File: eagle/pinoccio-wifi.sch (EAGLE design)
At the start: 18 parts, among them U1 LDO-TPS78233, U2 LDO-TPS73533

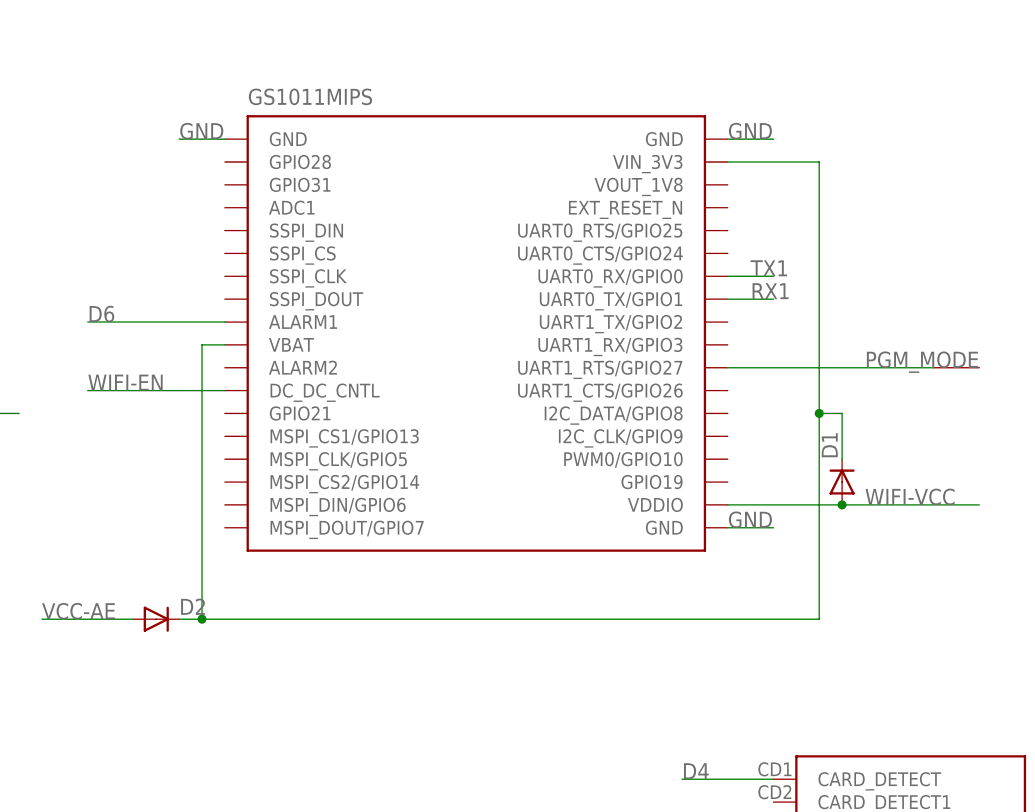
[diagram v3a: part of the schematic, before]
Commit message: Update datasheet and dioide layout to 0603
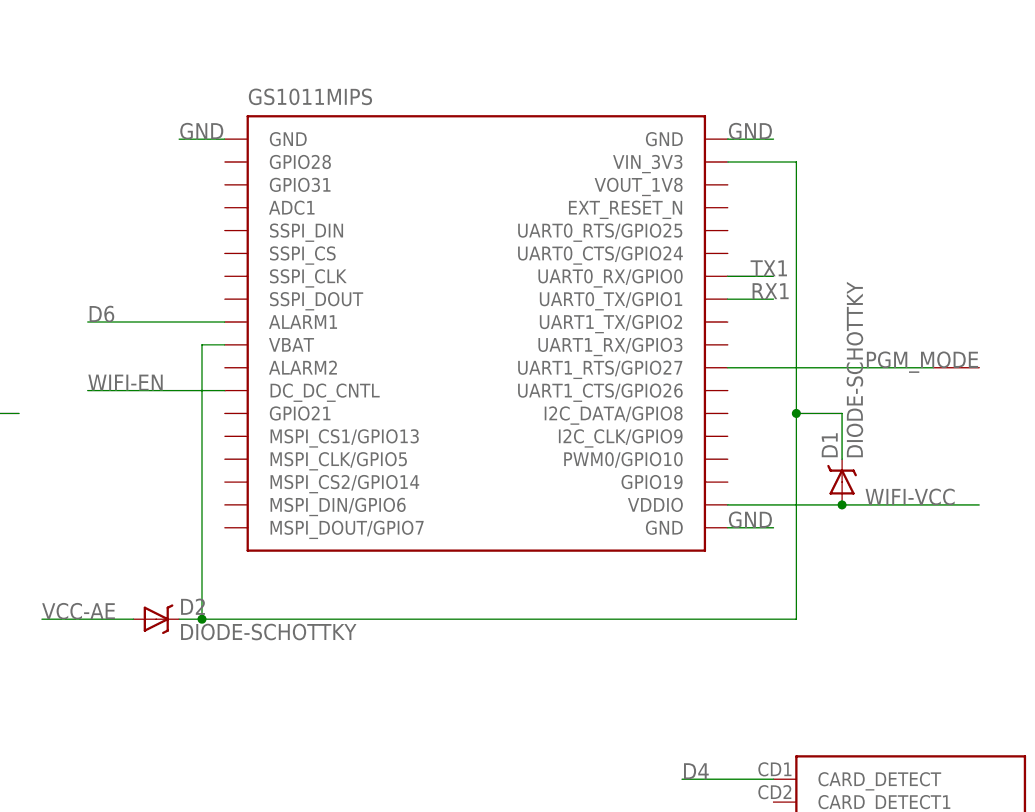
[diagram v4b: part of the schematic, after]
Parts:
- D1, D2: value (none) -> DIODE-SCHOTTKY; device Pinoccio:DIODE0603 -> Pinoccio:DIODE-SCHOTTKY
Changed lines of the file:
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@@
 <grid distance="0.1" unitdist="inch" unit="inch" style="lines" multiple="1" display="no" altdistance="0.01" altunitdist="inch" altunit="inch"/>
 <layers>
-<layer number="1" name="Top" color="4" fill="1" visible="yes" active="no"/>
-<layer number="2" name="Route2" color="1" fill="3" visible="yes" active="no"/>
-<layer number="3" name="Route3" color="4" fill="3" visible="yes" active="no"/>
-<layer number="4" name="Route4" color="1" fill="4" visible="yes" active="no"/>
-<layer number="5" name="Route5" color="4" fill="4" visible="yes" active="no"/>
-<layer number="6" name="Route6" color="1" fill="8" visible="yes" active="no"/>
-<layer number="7" name="Route7" color="4" fill="8" visible="yes" active="no"/>
-<layer number="8" name="Route8" color="1" fill="2" visible="yes" active="no"/>
-<layer number="9" name="Route9" color="4" fill="2" visible="yes" active="no"/>
-<layer number="10" name="Route10" color="1" fill="7" visible="yes" active="no"/>
-<layer number="11" name="Route11" color="4" fill="7" visible="yes" active="no"/>
-<layer number="12" name="Route12" color="1" fill="5" visible="yes" active="no"/>
-<layer number="13" name="Route13" color="4" fill="5" visible="yes" active="no"/>
-<layer number="14" name="Route14" color="1" fill="6" visible="yes" active="no"/>
-<layer number="15" name="Route15" color="4" fill="6" visible="yes" active="no"/>
-<layer number="16" name="Bottom" color="1" fill="1" visible="yes" active="no"/>
-<layer number="17" name="Pads" color="2" fill="1" visible="yes" active="no"/>
-<layer number="18" name="Vias" color="2" fill="1" visible="yes" active="no"/>
-<layer number="19" name="Unrouted" color="6" fill="1" visible="yes" active="no"/>
-<layer number="20" name="Dimension" color="6" fill="1" visible="yes" active="no"/>
-<layer number="21" name="tPlace" color="16" fill="1" visible="yes" active="no"/>
-<layer number="22" name="bPlace" color="14" fill="1" visible="yes" active="no"/>
-<layer number="23" name="tOrigins" color="15" fill="1" visible="yes" active="no"/>
-<layer number="24" name="bOrigins" color="15" fill="1" visible="yes" active="no"/>
-<layer number="25" name="tNames" color="7" fill="1" visible="yes" active="no"/>
-<layer number="26" name="bNames" color="7" fill="1" visible="yes" active="no"/>
-<layer number="27" name="tValues" color="7" fill="1" visible="yes" active="no"/>
-<layer number="28" name="bValues" color="7" fill="1" visible="yes" active="no"/>
+<layer number="1" name="Top" color="4" fill="1" visible="no" active="no"/>
+<layer number="2" name="Route2" color="1" fill="3" visible="no" active="no"/>
+<layer number="3" name="Route3" color="4" fill="3" visible="no" active="no"/>
+<layer number="4" name="Route4" color="1" fill="4" visible="no" active="no"/>
+<layer number="5" name="Route5" color="4" fill="4" visible="no" active="no"/>
+<layer number="6" name="Route6" color="1" fill="8" visible="no" active="no"/>
+<layer number="7" name="Route7" color="4" fill="8" visible="no" active="no"/>
+<layer number="8" name="Route8" color="1" fill="2" visible="no" active="no"/>
+<layer number="9" name="Route9" color="4" fill="2" visible="no" active="no"/>
+<layer number="10" name="Route10" color="1" fill="7" visible="no" active="no"/>
+<layer number="11" name="Route11" color="4" fill="7" visible="no" active="no"/>
+<layer number="12" name="Route12" color="1" fill="5" visible="no" active="no"/>
+<layer number="13" name="Route13" color="4" fill="5" visible="no" active="no"/>
+<layer number="14" name="Route14" color="1" fill="6" visible="no" active="no"/>
+<layer number="15" name="Route15" color="4" fill="6" visible="no" active="no"/>
+<layer number="16" name="Bottom" color="1" fill="1" visible="no" active="no"/>
+<layer number="17" name="Pads" color="2" fill="1" visible="no" active="no"/>
+<layer number="18" name="Vias" color="2" fill="1" visible="no" active="no"/>
+<layer number="19" name="Unrouted" color="6" fill="1" visible="no" active="no"/>
+<layer number="20" name="Dimension" color="6" fill="1" visible="no" active="no"/>
+<layer number="21" name="tPlace" color="16" fill="1" visible="no" active="no"/>
+<layer number="22" name="bPlace" color="14" fill="1" visible="no" active="no"/>
+<layer number="23" name="tOrigins" color="15" fill="1" visible="no" active="no"/>
+<layer number="24" name="bOrigins" color="15" fill="1" visible="no" active="no"/>
+<layer number="25" name="tNames" color="7" fill="1" visible="no" active="no"/>
+<layer number="26" name="bNames" color="7" fill="1" visible="no" active="no"/>
+<layer number="27" name="tValues" color="7" fill="1" visible="no" active="no"/>
+<layer number="28" name="bValues" color="7" fill="1" visible="no" active="no"/>
 <layer number="29" name="tStop" color="5" fill="1" visible="no" active="no"/>
 <layer number="30" name="bStop" color="7" fill="6" visible="no" active="no"/>
@@
 <layer number="35" name="tGlue" color="7" fill="4" visible="no" active="no"/>
 <layer number="36" name="bGlue" color="7" fill="5" visible="no" active="no"/>
-<layer number="37" name="tTest" color="7" fill="1" visible="yes" active="no"/>
-<layer number="38" name="bTest" color="7" fill="1" visible="yes" active="no"/>
+<layer number="37" name="tTest" color="7" fill="1" visible="no" active="no"/>
+<layer number="38" name="bTest" color="7" fill="1" visible="no" active="no"/>
 <layer number="39" name="tKeepout" color="4" fill="11" visible="no" active="no"/>
 <layer number="40" name="bKeepout" color="1" fill="11" visible="no" active="no"/>
@@
 <layer number="44" name="Drills" color="7" fill="1" visible="no" active="no"/>
 <layer number="45" name="Holes" color="7" fill="1" visible="no" active="no"/>
-<layer number="46" name="Milling" color="3" fill="1" visible="yes" active="no"/>
-<layer number="47" name="Measures" color="7" fill="1" visible="yes" active="no"/>
-<layer number="48" name="Document" color="7" fill="1" visible="yes" active="no"/>
-<layer number="49" name="Reference" color="7" fill="1" visible="yes" active="no"/>
-<layer number="50" name="dxf" color="7" fill="1" visible="yes" active="no"/>
-<layer number="51" name="tDocu" color="6" fill="1" visible="yes" active="no"/>
-<layer number="52" name="bDocu" color="7" fill="1" visible="yes" active="no"/>
-<layer number="53" name="tGND_GNDA" color="7" fill="9" visible="yes" active="no"/>
-<layer number="54" name="bGND_GNDA" color="1" fill="9" visible="yes" active="no"/>
-<layer number="56" name="wert" color="7" fill="1" visible="yes" active="no"/>
+<layer number="46" name="Milling" color="3" fill="1" visible="no" active="no"/>
+<layer number="47" name="Measures" color="7" fill="1" visible="no" active="no"/>
+<layer number="48" name="Document" color="7" fill="1" visible="no" active="no"/>
+<layer number="49" name="Reference" color="7" fill="1" visible="no" active="no"/>
+<layer number="50" name="dxf" color="7" fill="1" visible="no" active="no"/>
+<layer number="51" name="tDocu" color="6" fill="1" visible="no" active="no"/>
+<layer number="52" name="bDocu" color="7" fill="1" visible="no" active="no"/>
+<layer number="53" name="tGND_GNDA" color="7" fill="9" visible="no" active="no"/>
+<layer number="54" name="bGND_GNDA" color="1" fill="9" visible="no" active="no"/>
+<layer number="56" name="wert" color="7" fill="1" visible="no" active="no"/>
 <layer number="91" name="Nets" color="2" fill="1" visible="yes" active="yes"/>
 <layer number="92" name="Busses" color="1" fill="1" visible="yes" active="yes"/>
@@
 <part name="C2" library="Pinoccio" deviceset="CAP" device="0402-CAP" value="2.2uf"/>
 <part name="C4" library="Pinoccio" deviceset="CAP" device="0402-CAP" value="0.1uf"/>
-<part name="D1" library="Pinoccio" deviceset="DIODE" device="0603"/>
-<part name="D2" library="Pinoccio" deviceset="DIODE" device="0603"/>
+<part name="D1" library="Pinoccio" deviceset="DIODE-SCHOTTKY" device=""/>
+<part name="D2" library="Pinoccio" deviceset="DIODE-SCHOTTKY" device=""/>
 <part name="C3" library="Pinoccio" deviceset="CAP" device="0402-CAP" value="1.0uf"/>
 <part name="C6" library="Pinoccio" deviceset="CAP" device="0402-CAP" value="2.2uf"/>
@@
 <wire x1="111.76" y1="127" x2="109.22" y2="127" width="0.1524" layer="91"/>
 <wire x1="109.22" y1="127" x2="109.22" y2="96.52" width="0.1524" layer="91"/>
-<wire x1="109.22" y1="96.52" x2="177.8" y2="96.52" width="0.1524" layer="91"/>
-<wire x1="177.8" y1="96.52" x2="177.8" y2="119.38" width="0.1524" layer="91"/>
+<wire x1="109.22" y1="96.52" x2="175.26" y2="96.52" width="0.1524" layer="91"/>
+<wire x1="175.26" y1="96.52" x2="175.26" y2="119.38" width="0.1524" layer="91"/>
 <pinref part="GS1011MIPS" gate="GS1011MIPS" pin="VIN_3V3"/>
-<wire x1="177.8" y1="119.38" x2="177.8" y2="147.32" width="0.1524" layer="91"/>
-<wire x1="177.8" y1="147.32" x2="167.64" y2="147.32" width="0.1524" layer="91"/>
+<wire x1="175.26" y1="119.38" x2="175.26" y2="147.32" width="0.1524" layer="91"/>
+<wire x1="175.26" y1="147.32" x2="167.64" y2="147.32" width="0.1524" layer="91"/>
 <pinref part="D2" gate="G$1" pin="C"/>
 <wire x1="106.68" y1="96.52" x2="109.22" y2="96.52" width="0.1524" layer="91"/>
@@
 <pinref part="D1" gate="G$1" pin="C"/>
 <wire x1="180.34" y1="114.3" x2="180.34" y2="119.38" width="0.1524" layer="91"/>
-<wire x1="180.34" y1="119.38" x2="177.8" y2="119.38" width="0.1524" layer="91"/>
-<junction x="177.8" y="119.38"/>
+<wire x1="180.34" y1="119.38" x2="175.26" y2="119.38" width="0.1524" layer="91"/>
+<junction x="175.26" y="119.38"/>
 </segment>
 </net>

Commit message: v0.11 changes
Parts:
- removed D1, D2: DIODE-SCHOTTKY, Pinoccio:DIODE-SCHOTTKY
- removed U1: LDO-TPS78233, Pinoccio:LDO-TPS78233
- added C7: 0.1uf, Pinoccio:CAP0402-CAP
- added J1: AVR_SPI_PRG_6, Pinoccio:AVR_SPI_PRG_6
- added R2: 10k, Pinoccio:RESISTOR0402-RES
- added U$4: M25PX16SO8N, Pinoccio:M25PX16SO8N
- C3: value 1.0uf -> 0.1uf
- C5: value 10uf -> 22uf; device Pinoccio:CAP1206 -> Pinoccio:CAP0603-CAP
- C6: value 2.2uf -> 0.1uf
- U$2: value M25PX16 -> M25PX16SO8N; device Pinoccio:M25PX16 -> Pinoccio:M25PX16SO8N
- U$3: value PAD -> ATTINY13QFN10; device Pinoccio:PAD -> Pinoccio:ATTINY13QFN10
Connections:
- net USB_VIN renamed VBUS
- removed net D0: JP-L.10
- removed net D1: JP-L.11
- removed net MEM-VCC: C4.1, C5.1, C6.1, U$1.VDD, U$2.VCC, U1.OUT
- removed net PGM_MODE: GS1011MIPS.UART1_RTS/GPIO27, U$3.P$1
- removed net VBAT-AE: C1.1, C3.1, JP-R.3, U1.IN, U2.IN
- removed net WIFI-EN: GS1011MIPS.DC_DC_CNTL, U2.EN
- new net BKPK-BUS: J1.4, JP-L.2, U$3.PB0(MOSI)
- new net D7: GS1011MIPS.SSPI_CS, JP-L.15
- new net D8: JP-L.16, U$1.CS
- new net MSPI-CS: GS1011MIPS.MSPI_CS1/GPIO13, R2.2, U$4.!CS
- new net MSPI-MISO: GS1011MIPS.MSPI_DIN/GPIO6, U$4.SO
- new net MSPI-MOSI: GS1011MIPS.MSPI_DOUT/GPIO7, U$4.SI
- new net MSPI-SCK: GS1011MIPS.MSPI_CLK/GPIO5, U$4.SCK
- new net N$3: J1.3, U$3.PB2(SCK/ADC1)
- new net N$4: J1.5, U$3.PB5(NRES)
- new net VBAT: C1.1, JP-R.3, U2.IN
- net D2: now also JP-L.10; no longer JP-L.12
- net D3: now also JP-L.11; no longer JP-L.13
- net D4: now also JP-L.12; no longer JP-L.14, U$1.CARD_DETECT
- net D5: now also JP-L.13; no longer JP-L.15, U$1.CS
- net D6: now also GS1011MIPS.UART1_RTS/GPIO27, JP-L.14; no longer GS1011MIPS.ALARM1, JP-L.16
- net GND: now also C7.2, J1.6, U$3.GND, U$4.GND; no longer JP-L.2, U1.GND
- net MISO: now also GS1011MIPS.SSPI_DOUT
- net MOSI: now also GS1011MIPS.SSPI_DIN
- net N$2: now also J1.1, U$3.PB1(MISO); no longer D1.C, D2.C, GS1011MIPS.VBAT, GS1011MIPS.VIN_3V3
- net SCK: now also GS1011MIPS.SSPI_CLK
- net SSN: now also U$2.!CS; no longer U$2.CS
- net VCC-AE: now also C3.1, C4.1, C5.1, C7.1, GS1011MIPS.VBAT, GS1011MIPS.VIN_3V3, J1.2, U$1.VDD, U$2.VCC, U$3.VCC, U2.EN; no longer D2.A, U1.EN
- net WIFI-VCC: now also C6.1, R2.1, U$4.VCC; no longer D1.A
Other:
- note added: "0.11"
- note added: "Copyright Pinoccio 2012-2013"
- note removed: "0.9"
- note removed: "Copyright Pinoccio 2012"
- moved on the sheet: C1, C2, C3, C6, GS1011MIPS, U$2

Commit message: Updated board to v0.13
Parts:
- removed JP3, JP5: FIDUCIALUFIDUCIAL, Pinoccio:FIDUCIALUFIDUCIAL
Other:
- note added: "0.13"
- note removed: "0.11"
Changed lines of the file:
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@@
 <part name="JP-R" library="Pinoccio" deviceset="M16" device="2MM"/>
 <part name="JP-L" library="Pinoccio" deviceset="M16" device="2MM"/>
-<part name="JP3" library="Pinoccio" deviceset="FIDUCIAL" device="UFIDUCIAL"/>
-<part name="JP5" library="Pinoccio" deviceset="FIDUCIAL" device="UFIDUCIAL"/>
 <part name="GS1011MIPS" library="Pinoccio" deviceset="GS1011MIPS" device=""/>
 <part name="U$1" library="Pinoccio" deviceset="MICROSD" device=""/>
@@
 <sheet>
 <plain>
-<text x="238.76" y="1.27" size="2.54" layer="94" font="vector">0.11</text>
+<text x="238.76" y="1.27" size="2.54" layer="94" font="vector">0.13</text>
 <rectangle x1="0.38735" y1="0.29845" x2="0.41275" y2="0.31115" layer="21"/>
 <rectangle x1="0.36195" y1="0.31115" x2="0.45085" y2="0.32385" layer="21"/>
@@
 <instance part="JP-R" gate="G$1" x="243.84" y="104.14" rot="R180"/>
 <instance part="JP-L" gate="G$1" x="243.84" y="157.48" rot="R180"/>
-<instance part="JP3" gate="G$1" x="238.76" y="15.24"/>
-<instance part="JP5" gate="G$1" x="243.84" y="15.24"/>
 <instance part="GS1011MIPS" gate="GS1011MIPS" x="137.16" y="111.76"/>
 <instance part="U$1" gate="G$1" x="190.5" y="60.96"/>
